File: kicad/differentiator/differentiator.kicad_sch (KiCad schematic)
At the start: 6 parts, among them U1A TL082, U1B TL082

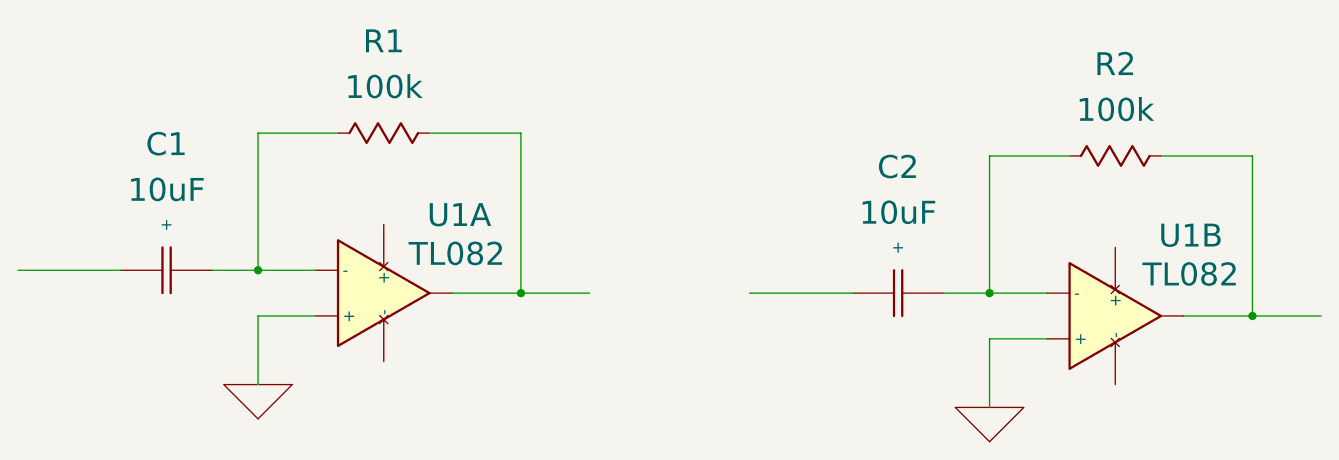
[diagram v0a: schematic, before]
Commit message: corrected input capacitor value
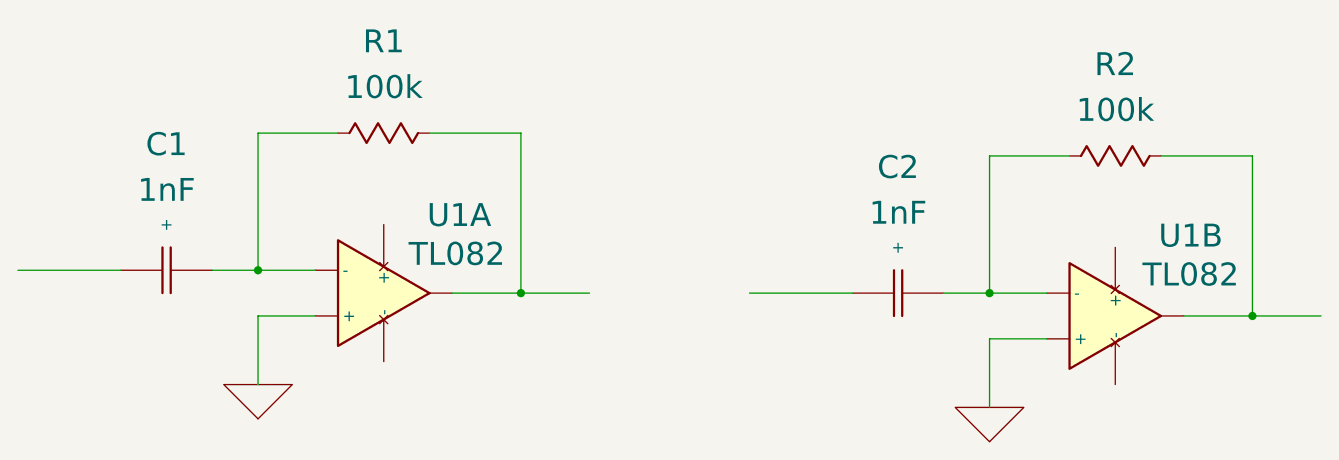
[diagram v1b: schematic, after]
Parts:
- C1, C2: value 10uF -> 1nF
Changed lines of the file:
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@@
 			)
 		)
-		(property "Value" "10uF"
+		(property "Value" "1nF"
 			(at 158.75 99.06 90)
 			(effects
@@
 			)
 		)
-		(property "Value" "10uF"
+		(property "Value" "1nF"
 			(at 77.47 96.52 90)
 			(effects
